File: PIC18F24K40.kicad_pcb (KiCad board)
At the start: 2 copper layers, 22 x 37.5 mm, 8 parts, among them J1 Conn_01x14, J2 Conn_01x14, J3 ICSP, U1 LM2931AD-5.0R2G, U2 PIC18F24K40-I_ML

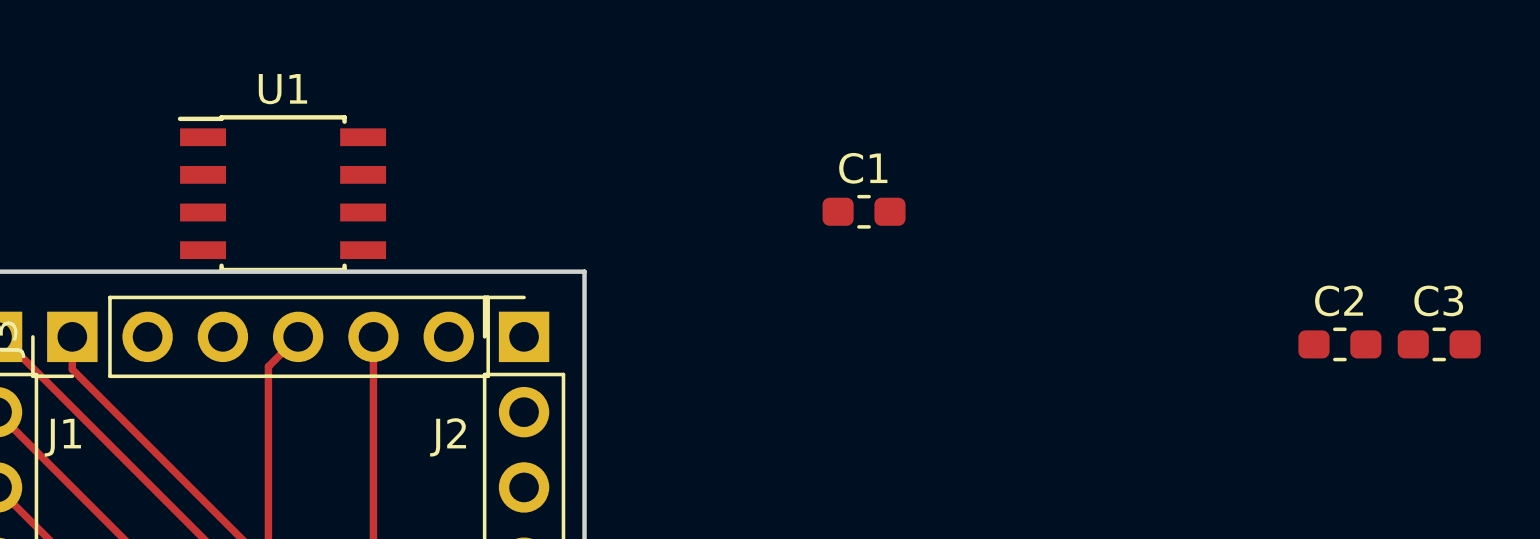
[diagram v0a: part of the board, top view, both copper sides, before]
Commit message: Regulator removed
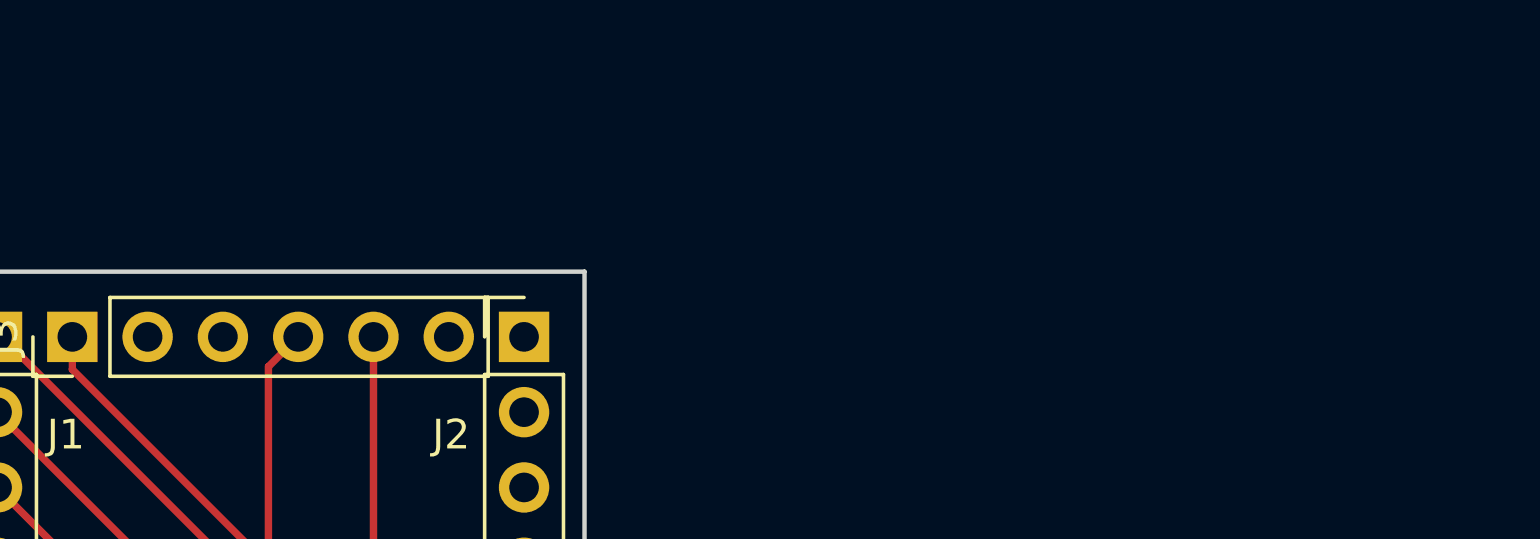
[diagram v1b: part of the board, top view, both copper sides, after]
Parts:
- removed C1, C3: 10uf, _PIC18F24K40:C_0603_1608Metric_Pad1.05x0.95mm_HandSolder
- removed C2: 0.1uf, _PIC18F24K40:C_0603_1608Metric_Pad1.05x0.95mm_HandSolder
- removed U1: LM2931AD-5.0R2G, _PIC18F24K40:SOIC-8_3.9x4.9mm_P1.27mm

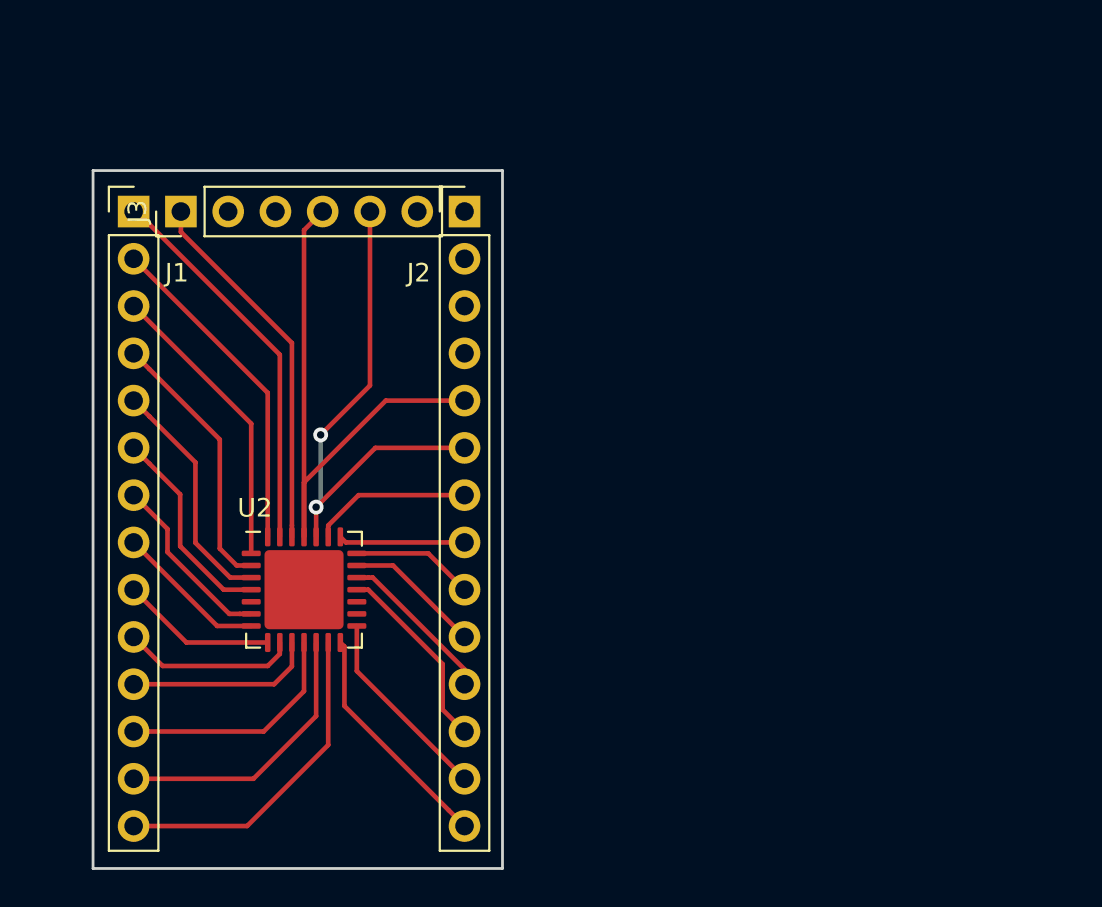
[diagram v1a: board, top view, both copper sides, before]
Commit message: Mostly cleanup
Backup and cache files are no longer versioned.

I've changed the breakout headers to 13 pin from 14 as we don't need
multiple power and ground pins broken out.

I think this board will be much more useful if it has the ability to
talk to a computer, so I'll be adding a part for the FTDI chip in the
reference folder, along with a USB type ? connector.

Currently the board is spaced to fit in a breadboard rather than
compatible with the arduino standard.
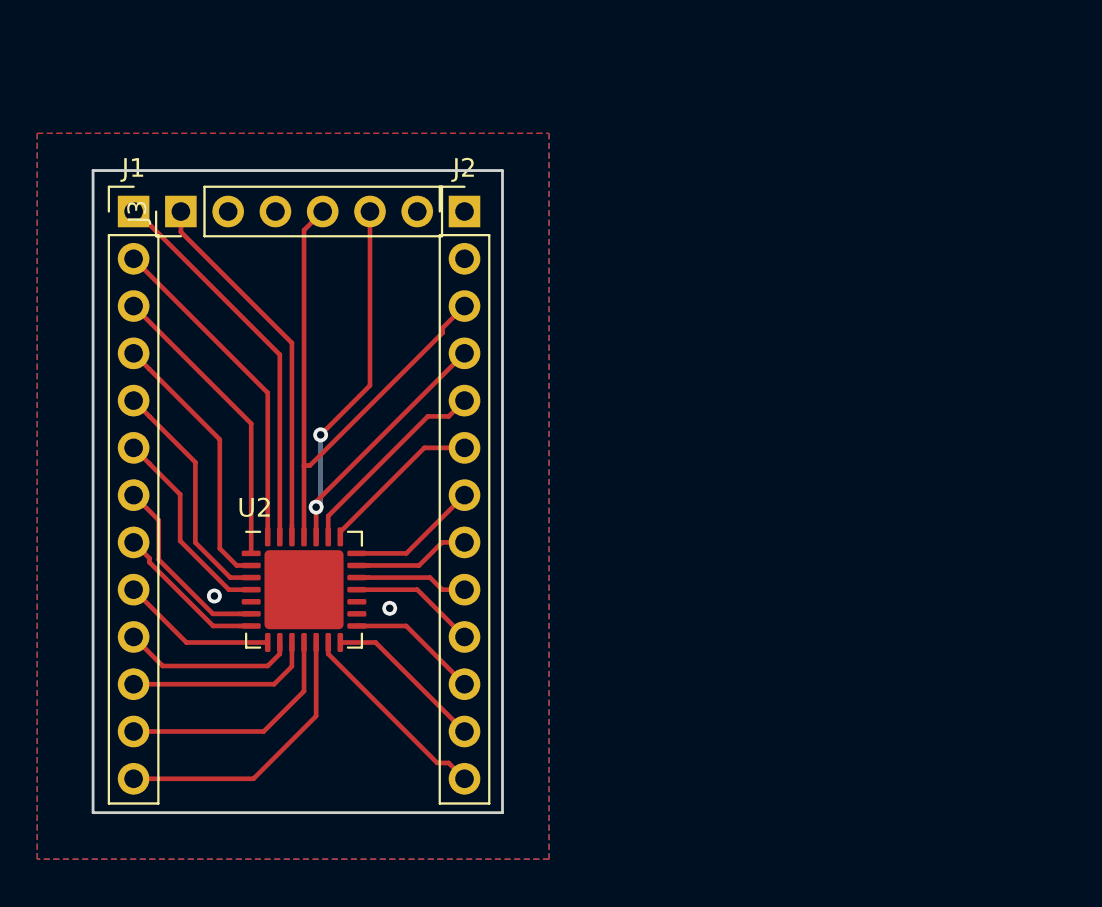
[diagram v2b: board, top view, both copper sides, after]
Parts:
- J1, J2: value Conn_01x14 -> Conn_01x13; footprint _PIC18F24K40:PinHeader_1x14_P2.54mm_Vertical -> _PIC18F24K40:PinHeader_1x13_P2.54mm_Vertical
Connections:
- J2 pad 1: Net-(J2-Pad1) -> VCC
- J2 pad 10: /RB2 -> /RB0
- J2 pad 11: /RB1 -> /RC7
- J2 pad 12: /RB0 -> /RC6
- J2 pad 13: /RC7 -> /RC5
- J2 pad 2: Net-(J2-Pad2) -> GND
- J2 pad 3: Net-(J2-Pad3) -> /RB7
- J2 pad 4: Net-(J2-Pad4) -> /RB6
- J2 pad 5: /RB7 -> /RB5
- J2 pad 6: /RB6 -> /RB4
- J2 pad 7: /RB5 -> /RB3
- J2 pad 8: /RB4 -> /RB2
- J2 pad 9: /RB3 -> /RB1
- U2 pad 16: Net-(U2-Pad16) -> GND
- U2 pad 17: Net-(U2-Pad17) -> VCC
- U2 pad 5: Net-(U2-Pad5) -> GND
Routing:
- net /RC5: track 17.8 -> 10.7 mm
- net /RC6: track 12.6 -> 8.66 mm
- net /RB0: track 10.4 -> 6.84 mm
- net /RC7: track 10.6 -> 7.08 mm
- net /RB1: track 8.63 -> 6.06 mm
- net /RB5: track 8.61 -> 11.0 mm
- net /RB6: track 28.0 -> 30.2 mm
- net /RB4: track 6.80 -> 8.81 mm
- net /RB2: track 7.38 -> 6.30 mm
- net /RB7: track 31.3 -> 30.2 mm
- net /RA6: track 9.69 -> 10.2 mm
- net GND: vias 0 -> 2
- added copper zone on B.Cu, net GND
- added copper zone on F.Cu, net GND
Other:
- board size 22 x 37.5 mm -> 22 x 34.5 mm

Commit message: Basic layout and schematic capture
SCH:
- added decoupling cap for micro

PCB:
- fill on top layer removed
- decoupling cap placed next to micro

MODEL:
- 1x13 header model flipped to represent the down facing orientation
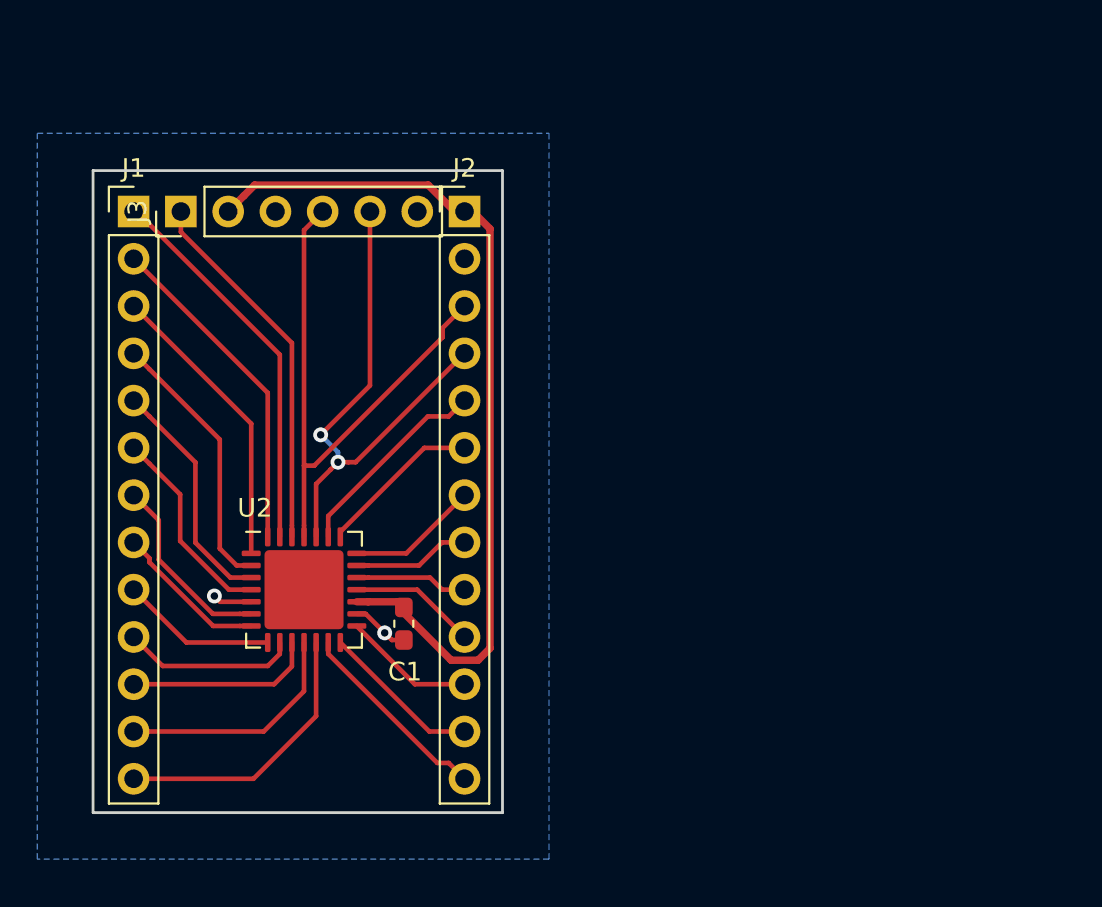
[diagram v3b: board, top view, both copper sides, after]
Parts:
- added C1: 0.1uf, _PIC18F24K40:C_0603_1608Metric_Pad1.05x0.95mm_HandSolder, F.Cu at (121.2, 98.3)
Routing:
- net VCC: track 0.00 -> 47.1 mm
- net GND: track 0.00 -> 5.22 mm
- net /RB6: track 30.2 -> 28.7 mm
- removed copper zone on F.Cu, net GND
